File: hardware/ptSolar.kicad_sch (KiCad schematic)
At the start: 52 parts, among them J3 Conn_01x03, J4 ICSP, J5 Qwiic, U2 SA818S-V, U3 TXB0104D, U4 BME280, U5 LP3985IM5-3.3/NOPB, U7 MEGA8-AI, Y2 8MHz

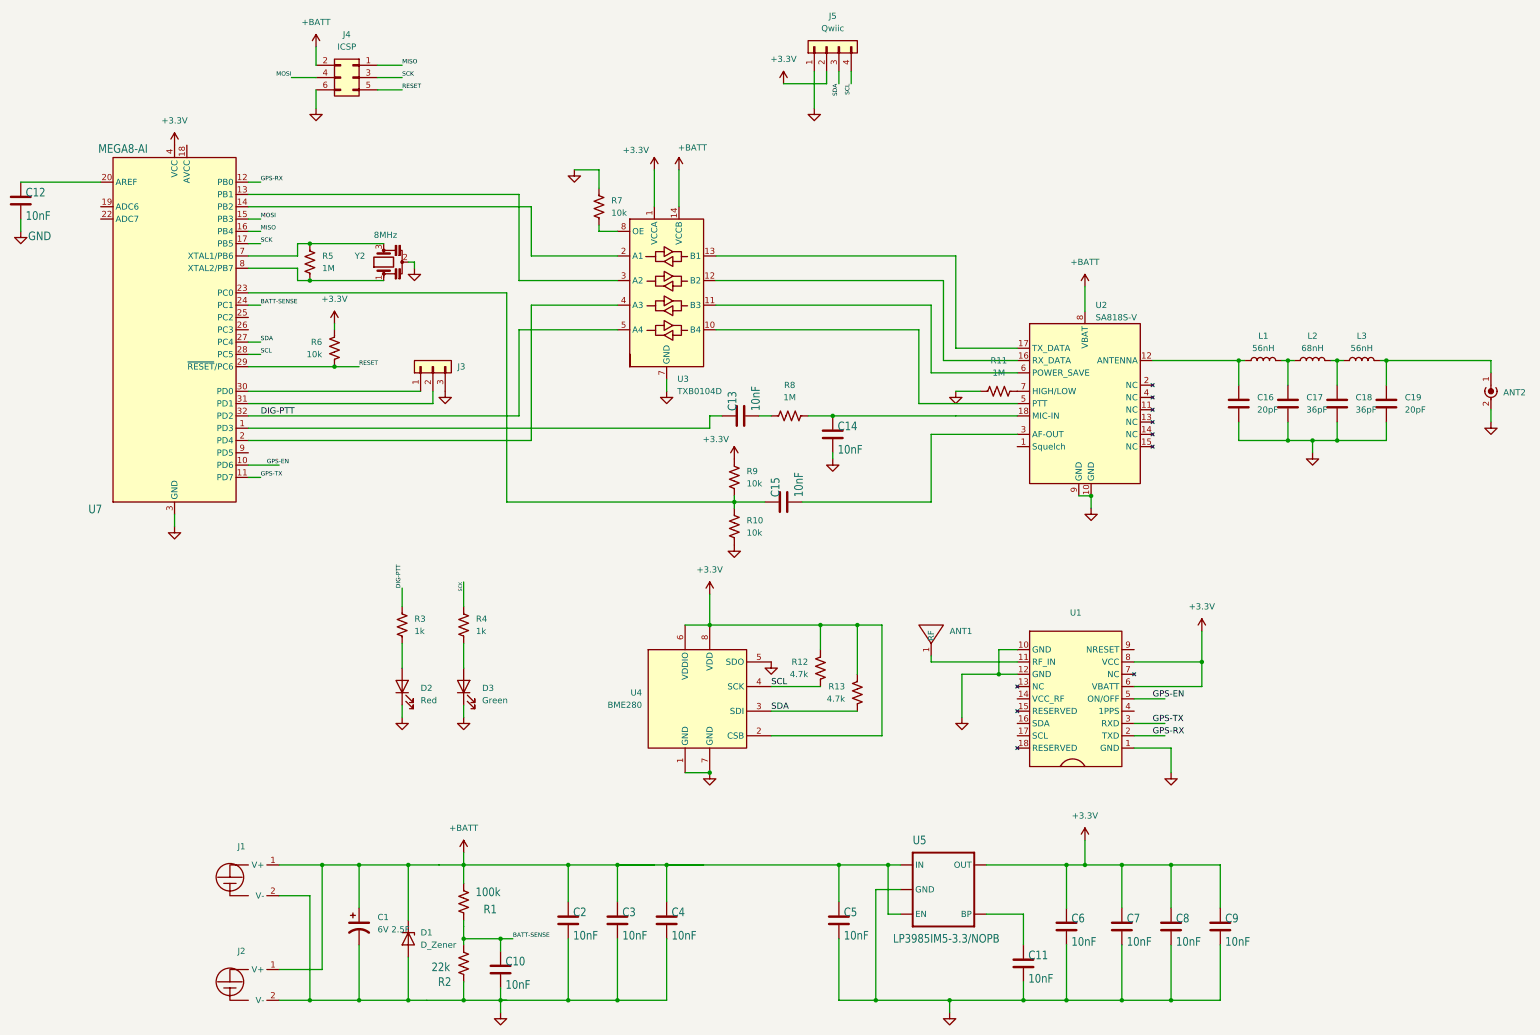
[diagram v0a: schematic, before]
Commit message: Updated to PCB 1.1.0. Firmware mostly validated. Switched to FET-based level translators.
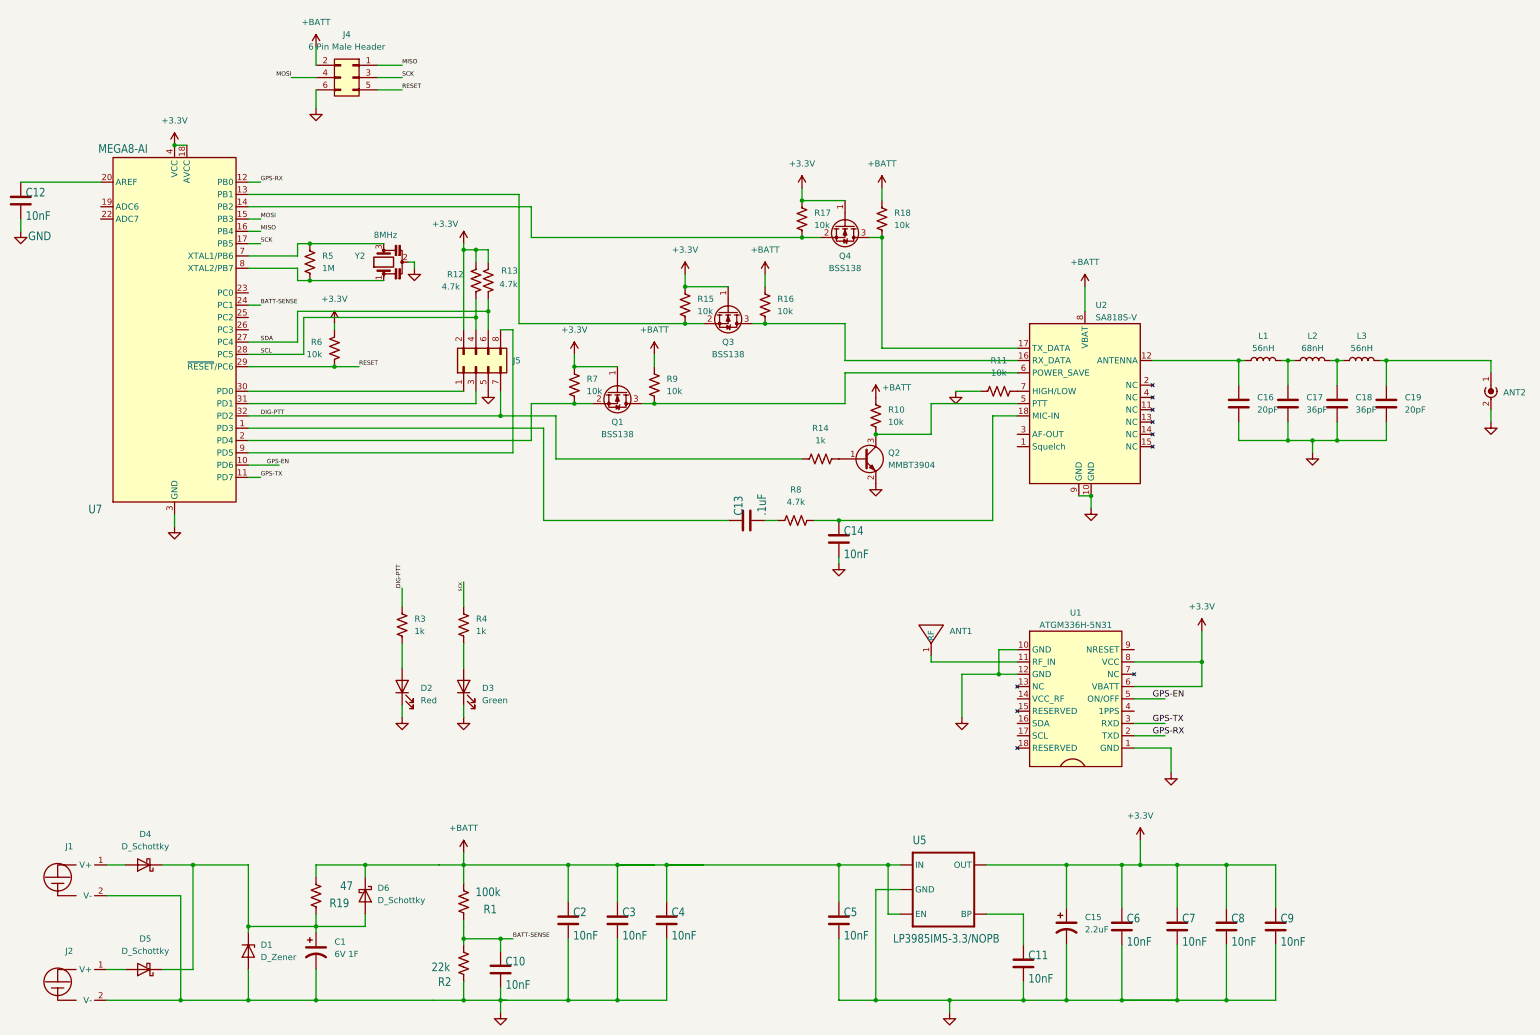
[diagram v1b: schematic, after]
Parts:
- removed C15: 10nF, Capacitor_SMD:C_0805_2012Metric, symbol Device:C
- removed J3: Conn_01x03, Connector_PinHeader_2.54mm:PinHeader_1x03_P2.54mm_Vertical, symbol Connector_Generic:Conn_01x03
- removed J5: Qwiic, Connector_JST:JST_SH_SM04B-SRSS-TB_1x04-1MP_P1.00mm_Horizontal, symbol Connector_Generic:Conn_01x04
- removed U3: TXB0104D, Package_SO:SOIC-14_3.9x8.7mm_P1.27mm, symbol Logic_LevelTranslator:TXB0104D
- removed U4: BME280, Package_LGA:Bosch_LGA-8_2.5x2.5mm_P0.65mm_ClockwisePinNumbering, symbol Sensor:BME280
- added C15: 2.2uF, Capacitor_SMD:C_0805_2012Metric, symbol Device:C_Polarized_US
- added D4, D5, D6: D_Schottky, Diode_SMD:D_SMA, symbol Device:D_Schottky
- added J5: Conn_02x04_Odd_Even, Connector_PinHeader_2.54mm:PinHeader_2x04_P2.54mm_Vertical, symbol Connector_Generic:Conn_02x04_Odd_Even
- added Q1, Q3, Q4: BSS138, Package_TO_SOT_SMD:SOT-23, symbol Transistor_FET:BSS138
- added Q2: MMBT3904, Package_TO_SOT_SMD:SOT-23, symbol Transistor_BJT:MMBT3904
- added R14: 1k, Resistor_SMD:R_0805_2012Metric, symbol Device:R_US
- added R15, R16, R17, R18: 10k, Resistor_SMD:R_0805_2012Metric, symbol Device:R_US
- added R19: 47, Resistor_SMD:R_2512_6332Metric, symbol Device:R_US
- ANT2: value Conn_Coaxial_Power -> SMA Edge Mount (Optional); footprint Connector_Coaxial:SMA_Amphenol_132289_EdgeMount -> Connector_Coaxial:SMA_Samtec_SMA-J-P-H-ST-EM1_EdgeMount
- C1: value 6V 2.5F -> 6V 1F; footprint Capacitor_THT:CP_Radial_D16.0mm_P7.50mm -> Custom DS:CDS CSP Super Cap 8mm dia; Digikey (none) -> TBD2
- C13: value 10nF -> .1uF; Digikey 399-1158-1-ND -> (none)
- J4: value ICSP -> 6 Pin Male Header; footprint Connector_PinHeader_2.00mm:PinHeader_2x03_P2.00mm_Vertical -> Connector_PinHeader_2.54mm:PinHeader_2x03_P2.54mm_Vertical
- R1: DIGIKEY 311-100KCRCT-ND -> (none); Digikey (none) -> 311-100KCRCT-ND
- R10, R6, R7, R9: Digikey (none) -> 311-10KARCT-ND
- R11: value 1M -> 10k; Digikey 311-1.0MARCT-ND -> 311-10KARCT-ND
- R12, R13: Digikey (none) -> 311-4.7KARCT-ND
- R2: Digikey (none) -> 311-22KARTR-ND
- R8: value 1M -> 4.7k; Digikey 311-1.0MARCT-ND -> 311-4.7KARCT-ND
- U1: value ~ -> ATGM336H-5N31; Digikey (none) -> ALIEXPRESS
- U2: Digikey (none) -> ALIEXPRESS
- U7: DIGIKEY ATMEGA328P-AU-ND -> (none); Digikey (none) -> ATMEGA328P-AU-ND
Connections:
- net +3.3V: now also R7.2, U7.18 (AVCC), C15.1, J5.2 (Pin_2), Q1.1 (G), Q3.1 (G), Q4.1 (G), R15.2, R17.2; no longer R9.1
- net +BATT: now also R10.2, R9.2, D6.1 (K), R16.2, R18.2, R19.2; no longer C1.1, D1.1 (K), J1.1 (V+), J2.1 (V+)
- net DIG-PTT: now also J5.7 (Pin_7), R14.1
- net GND: now also C15.2, J5.5 (Pin_5), Q2.2 (E); no longer R10.2, R7.1
- net SCL: now also J5.4 (Pin_4)
- net SDA: now also J5.6 (Pin_6)
- net at U7.13 (PB1): now also Q3.2 (S), R15.1
- net at U7.14 (PB2): now also Q4.2 (S), R17.1
- net at U7.2 (PD4): now also R7.1, Q1.2 (S)
- net at U7.30 (PD0): now also J5.1 (Pin_1)
- net at U7.31 (PD1): now also J5.3 (Pin_3)
- net at U7.9 (PD5): now also J5.8 (Pin_8)
- net at U2.16 (RX_DATA): now also Q3.3 (D), R16.1
- net at U2.17 (TX_DATA): now also Q4.3 (D), R18.1
- net at U2.5 (PTT): now also R10.1, Q2.3 (C)
- net at U2.6 (POWER_SAVE): now also R9.1, Q1.3 (D)
- new net: C1.1, D1.1 (K), D4.1 (K), D5.1 (K), D6.2 (A), R19.1
- new net: Q2.1 (B), R14.2
- new net: D5.2 (A), J2.1 (V+)
- new net: D4.2 (A), J1.1 (V+)
- now unconnected: U7.23 (PC0)
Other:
- moved on the sheet: C1, C13, C14, C6, C7, C8, C9, D1, J1, J2, R8
